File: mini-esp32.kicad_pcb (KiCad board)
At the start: 4 copper layers, 29 x 58 mm, 52 parts, among them J1 BAT, J2 USB_B_Micro, J5 Conn_01x18, J6 Conn_01x18, Q1 AO3401A, Q2 S8050, Q3 S8050, Q5 AO3400A, Q6 AO3400A, SW1 RESET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

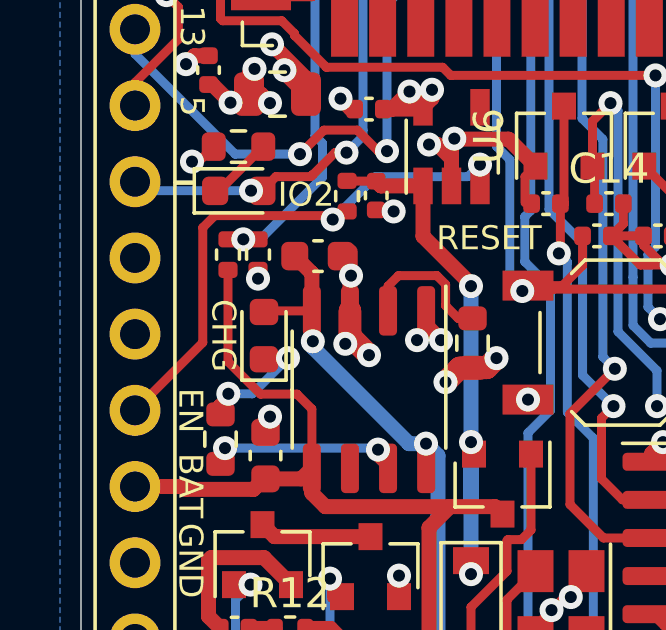
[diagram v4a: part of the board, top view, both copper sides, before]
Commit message: Lower leakage current on battery voltage divider. Add caps.
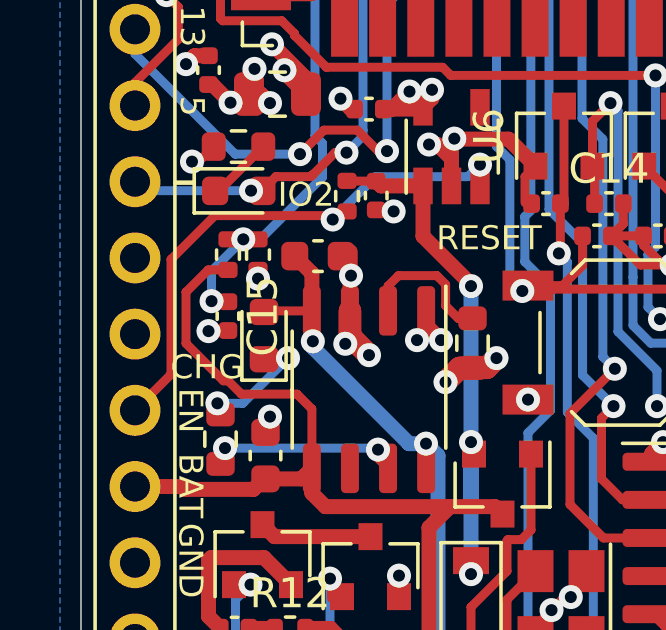
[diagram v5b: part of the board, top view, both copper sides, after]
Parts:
- added C15: 100n, Capacitor_SMD:C_0402_1005Metric, F.Cu at (124.1, 96.4)
- R5, R6: value 100k -> 1M
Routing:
- net I35: track 45.6 -> 48.6 mm, vias 4 -> 5
- net BAT+: track 39.9 -> 41.9 mm
- net GND: track 52.9 -> 53.6 mm, vias 34 -> 35
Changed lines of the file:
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@@
     (thickness 1.6)
     (drawings 81)
-    (tracks 818)
+    (tracks 830)
     (zones 0)
-    (modules 52)
+    (modules 53)
     (nets 79)
   )
@@
   )
   (setup
-    (last_trace_width 0.75)
+    (last_trace_width 0.3)
     (user_trace_width 0.3)
     (user_trace_width 0.5)
@@
       (effects (font (size 1 1) (thickness 0.15)))
     )
-    (fp_text value 100k (at 0 1.17 90) (layer F.Fab)
+    (fp_text value 1M (at 0 1.17 90) (layer F.Fab)
       (effects (font (size 1 1) (thickness 0.15)))
     )
@@
       (effects (font (size 1 1) (thickness 0.15)))
     )
-    (fp_text value 100k (at 0 1.17 90) (layer F.Fab)
+    (fp_text value 1M (at 0 1.17 90) (layer F.Fab)
       (effects (font (size 1 1) (thickness 0.15)))
     )
@@
     )
   )
+  (module Capacitor_SMD:C_0402_1005Metric (layer F.Cu)
+    (at 124.1 96.4 270)
+    (descr "Capacitor SMD 0402 (1005 Metric), square (rectangular) end terminal, IPC_7351 nominal, (Body size source: IPC-SM-782 page 76, https://www.pcb-3d.com/wordpress/wp-content/uploads/ipc-sm-782a_amendment_1_and_2.pdf), generated with kicad-footprint-generator")
+    (tags capacitor)
+    (attr smd)
+    (fp_text reference C15 (at 0 -1.16 90) (layer F.SilkS)
+      (effects (font (size 1 1) (thickness 0.15)))
+    )
+    (fp_text value 100n (at 0 1.16 90) (layer F.Fab)
+      (effects (font (size 1 1) (thickness 0.15)))
+    )
+    (fp_line (start 0.91 0.46) (end -0.91 0.46) (layer F.CrtYd) (width 0.05))
+    (fp_line (start 0.91 -0.46) (end 0.91 0.46) (layer F.CrtYd) (width 0.05))
+    (fp_line (start -0.91 -0.46) (end 0.91 -0.46) (layer F.CrtYd) (width 0.05))
+    (fp_line (start -0.91 0.46) (end -0.91 -0.46) (layer F.CrtYd) (width 0.05))
+    (fp_line (start -0.107836 0.36) (end 0.107836 0.36) (layer F.SilkS) (width 0.12))
+    (fp_line (start -0.107836 -0.36) (end 0.107836 -0.36) (layer F.SilkS) (width 0.12))
+    (fp_line (start 0.5 0.25) (end -0.5 0.25) (layer F.Fab) (width 0.1))
+    (fp_line (start 0.5 -0.25) (end 0.5 0.25) (layer F.Fab) (width 0.1))
+    (fp_line (start -0.5 -0.25) (end 0.5 -0.25) (layer F.Fab) (width 0.1))
+    (fp_line (start -0.5 0.25) (end -0.5 -0.25) (layer F.Fab) (width 0.1))
+    (fp_text user %R (at 0 0 90) (layer F.Fab)
+      (effects (font (size 0.25 0.25) (thickness 0.04)))
+    )
+    (pad 1 smd roundrect (at -0.48 0 270) (size 0.56 0.62) (layers F.Cu F.Paste F.Mask) (roundrect_rratio 0.25)
+      (net 41 I35))
+    (pad 2 smd roundrect (at 0.48 0 270) (size 0.56 0.62) (layers F.Cu F.Paste F.Mask) (roundrect_rratio 0.25)
+      (net 2 GND))
+    (model ${KISYS3DMOD}/Capacitor_SMD.3dshapes/C_0402_1005Metric.wrl
+      (at (xyz 0 0 0))
+      (scale (xyz 1 1 1))
+      (rotate (xyz 0 0 0))
+    )
+  )
   (gr_text RST (at 143.8148 112.2426 180) (layer B.SilkS)
     (effects (font (size 0.8 0.8) (thickness 0.15)) (justify mirror))
@@
     (effects (font (size 0.8 0.8) (thickness 0.15)))
   )
-  (gr_text CHG (at 123.95 97.05 270) (layer F.SilkS)
+  (gr_text CHG (at 123.4 98.1) (layer F.SilkS)
     (effects (font (size 0.8 0.8) (thickness 0.15)))
   )
@@
   (segment (start 128.165 97.065) (end 128.800008 97.700008) (width 0.75) (layer F.Cu) (net 2))
   (segment (start 128.165 96.225) (end 128.165 97.065) (width 0.75) (layer F.Cu) (net 2))
+  (via (at 123.450022 96.9) (size 0.8) (drill 0.4) (layers F.Cu B.Cu) (net 2))
+  (segment (start 123.470022 96.88) (end 123.450022 96.9) (width 0.3) (layer F.Cu) (net 2))
+  (segment (start 124.1 96.88) (end 123.470022 96.88) (width 0.3) (layer F.Cu) (net 2))
   (via (at 132.2 105) (size 0.8) (drill 0.4) (layers F.Cu B.Cu) (net 3))
   (segment (start 132.2 104.55) (end 132.2 105) (width 0.5) (layer F.Cu) (net 3))
@@
   (segment (start 133.430003 103.849999) (end 133.880003 103.849999) (width 0.3) (layer F.Cu) (net 8))
   (segment (start 133.399999 103.880003) (end 133.430003 103.849999) (width 0.3) (layer F.Cu) (net 8))
-  (via (at 124.111244 98.988756) (size 0.8) (drill 0.4) (layers F.Cu B.Cu) (net 9))
-  (segment (start 123.75 99.35) (end 124.111244 98.988756) (width 0.3) (layer F.Cu) (net 9))
   (via (at 126.1 97.8) (size 0.8) (drill 0.4) (layers F.Cu B.Cu) (net 9))
-  (segment (start 124.911244 98.988756) (end 126.1 97.8) (width 0.3) (layer B.Cu) (net 9))
-  (segment (start 124.111244 98.988756) (end 124.911244 98.988756) (width 0.3) (layer B.Cu) (net 9))
   (segment (start 125.3375 97.8) (end 125.3 97.8375) (width 0.3) (layer F.Cu) (net 9))
   (segment (start 126.1 97.8) (end 125.3375 97.8) (width 0.3) (layer F.Cu) (net 9))
-  (segment (start 123.75 99.675) (end 123.75 99.35) (width 0.3) (layer F.Cu) (net 9))
+  (segment (start 124.593178 99.306822) (end 123.746147 99.306822) (width 0.3) (layer B.Cu) (net 9))
+  (segment (start 123.75 99.310675) (end 123.746147 99.306822) (width 0.3) (layer F.Cu) (net 9))
+  (segment (start 126.1 97.8) (end 124.593178 99.306822) (width 0.3) (layer B.Cu) (net 9))
+  (segment (start 123.75 99.675) (end 123.75 99.310675) (width 0.3) (layer F.Cu) (net 9))
+  (via (at 123.746147 99.306822) (size 0.8) (drill 0.4) (layers F.Cu B.Cu) (net 9))
   (segment (start 123.825 92.2) (end 125.275 90.75) (width 0.3) (layer F.Cu) (net 10))
   (segment (start 123.6725 92.2) (end 123.825 92.2) (width 0.3) (layer F.Cu) (net 10))
@@
   (segment (start 137.906156 112.822164) (end 137.906156 113.120155) (width 0.261112) (layer F.Cu) (net 13))
   (segment (start 140.832156 109.896164) (end 137.906156 112.822164) (width 0.261112) (layer F.Cu) (net 13))
-  (segment (start 127.46001 93.05001) (end 127.59 93.18) (width 0.3) (layer F.Cu) (net 15))
-  (segment (start 123.65999 93.05001) (end 127.46001 93.05001) (width 0.3) (layer F.Cu) (net 15))
-  (segment (start 121 99.54) (end 123.26 97.28) (width 0.3) (layer F.Cu) (net 15))
-  (segment (start 123.26 93.45) (end 123.65999 93.05001) (width 0.3) (layer F.Cu) (net 15))
-  (segment (start 123.26 97.28) (end 123.26 93.45) (width 0.3) (layer F.Cu) (net 15))
   (segment (start 127.66 93.25) (end 127.59 93.18) (width 0.3) (layer B.Cu) (net 15))
   (via (at 127.59 93.18) (size 0.8) (drill 0.4) (layers F.Cu B.Cu) (net 15))
@@
   (segment (start 129.01999 91.75001) (end 132.100067 91.75001) (width 0.3) (layer B.Cu) (net 15))
   (segment (start 127.59 93.18) (end 129.01999 91.75001) (width 0.3) (layer B.Cu) (net 15))
+  (segment (start 121 99.54) (end 122.200001 98.339999) (width 0.3) (layer F.Cu) (net 15))
+  (segment (start 122.200001 94.509999) (end 123.65999 93.05001) (width 0.3) (layer F.Cu) (net 15))
+  (segment (start 123.65999 93.05001) (end 127.46001 93.05001) (width 0.3) (layer F.Cu) (net 15))
+  (segment (start 127.46001 93.05001) (end 127.59 93.18) (width 0.3) (layer F.Cu) (net 15))
+  (segment (start 122.200001 98.339999) (end 122.200001 94.509999) (width 0.3) (layer F.Cu) (net 15))
   (via (at 137.6 83) (size 0.8) (drill 0.4) (layers F.Cu B.Cu) (net 16))
   (via (at 137.6 75.6) (size 0.8) (drill 0.4) (layers F.Cu B.Cu) (net 16))
@@
   (segment (start 139.4 77.75) (end 139.4 76.889998) (width 0.3) (layer B.Cu) (net 41))
   (segment (start 139.4 76.889998) (end 140.889998 75.4) (width 0.3) (layer B.Cu) (net 41))
+  (segment (start 123.570181 95.92) (end 123.551496 95.901315) (width 0.3) (layer F.Cu) (net 41))
+  (segment (start 124.1 95.92) (end 123.570181 95.92) (width 0.3) (layer F.Cu) (net 41))
+  (segment (start 124.610002 93.84) (end 123.551496 94.898506) (width 0.3) (layer B.Cu) (net 41))
+  (segment (start 123.551496 94.898506) (end 123.551496 95.901315) (width 0.3) (layer B.Cu) (net 41))
+  (via (at 123.551496 95.901315) (size 0.8) (drill 0.4) (layers F.Cu B.Cu) (net 41))
   (via (at 128.8 68.5) (size 0.8) (drill 0.4) (layers F.Cu B.Cu) (net 42))
   (segment (start 128.855001 68.444999) (end 128.8 68.5) (width 0.3) (layer F.Cu) (net 42))
@@
   (segment (start 129.6 113.064968) (end 129.6 114.5) (width 0.5) (layer F.Cu) (net 68))
   (segment (start 122.58 102.08) (end 121 102.08) (width 0.5) (layer F.Cu) (net 68))
-  (segment (start 126.895 101.475) (end 126.895 99.495) (width 0.3) (layer F.Cu) (net 68))
-  (segment (start 126.895 99.495) (end 126.4 99) (width 0.3) (layer F.Cu) (net 68))
-  (segment (start 125.18315 99) (end 124.1 97.91685) (width 0.3) (layer F.Cu) (net 68))
-  (segment (start 124.1 97.91685) (end 124.1 94.86) (width 0.3) (layer F.Cu) (net 68))
-  (segment (start 126.4 99) (end 125.18315 99) (width 0.3) (layer F.Cu) (net 68))
   (segment (start 126.545 101.825) (end 126.895 101.475) (width 0.5) (layer F.Cu) (net 68))
   (segment (start 125.3 101.825) (end 126.545 101.825) (width 0.5) (layer F.Cu) (net 68))
@@
   (segment (start 127.518002 106.81) (end 126.68 106.81) (width 0.5) (layer F.Cu) (net 68))
   (segment (start 129.6 108.891998) (end 127.518002 106.81) (width 0.5) (layer F.Cu) (net 68))
+  (segment (start 126.4 99) (end 124.549327 99) (width 0.3) (layer F.Cu) (net 68))
+  (segment (start 122.700012 97.310016) (end 122.700012 95.599988) (width 0.3) (layer F.Cu) (net 68))
+  (segment (start 123.44 94.86) (end 124.1 94.86) (width 0.3) (layer F.Cu) (net 68))
+  (segment (start 126.895 101.475) (end 126.895 99.495) (width 0.3) (layer F.Cu) (net 68))
+  (segment (start 122.700012 95.599988) (end 123.44 94.86) (width 0.3) (layer F.Cu) (net 68))
+  (segment (start 126.895 99.495) (end 126.4 99) (width 0.3) (layer F.Cu) (net 68))
+  (segment (start 124.106148 98.556821) (end 123.946817 98.556821) (width 0.3) (layer F.Cu) (net 68))
+  (segment (start 124.549327 99) (end 124.106148 98.556821) (width 0.3) (layer F.Cu) (net 68))
+  (segment (start 123.946817 98.556821) (end 122.700012 97.310016) (width 0.3) (layer F.Cu) (net 68))
   (segment (start 127.1 114) (end 127.6 114.5) (width 0.5) (layer F.Cu) (net 69))
   (segment (start 127.1 109.534998) (end 127.1 114) (width 0.5) (layer F.Cu) (net 69))

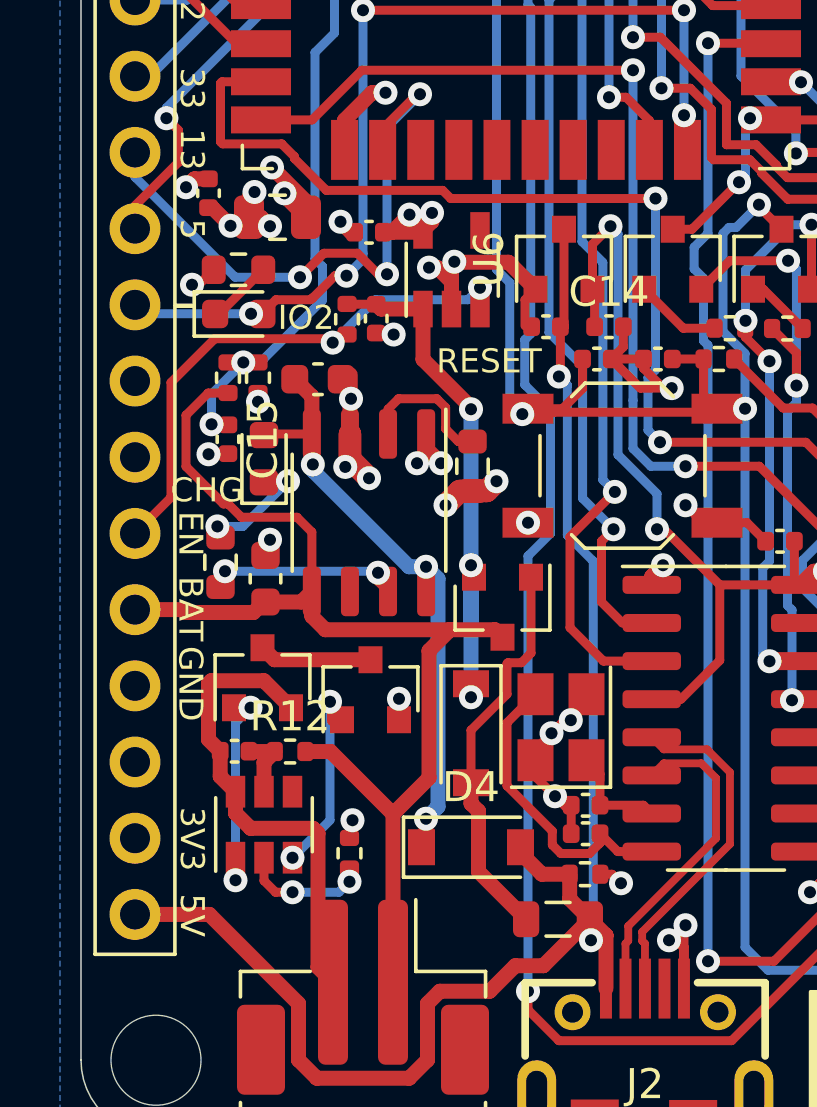
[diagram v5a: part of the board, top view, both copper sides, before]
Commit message: Fix EN pin cap to increase startup delay. Cheaper main bulk cap.
Improve thermals for D4 diode. (For charging)
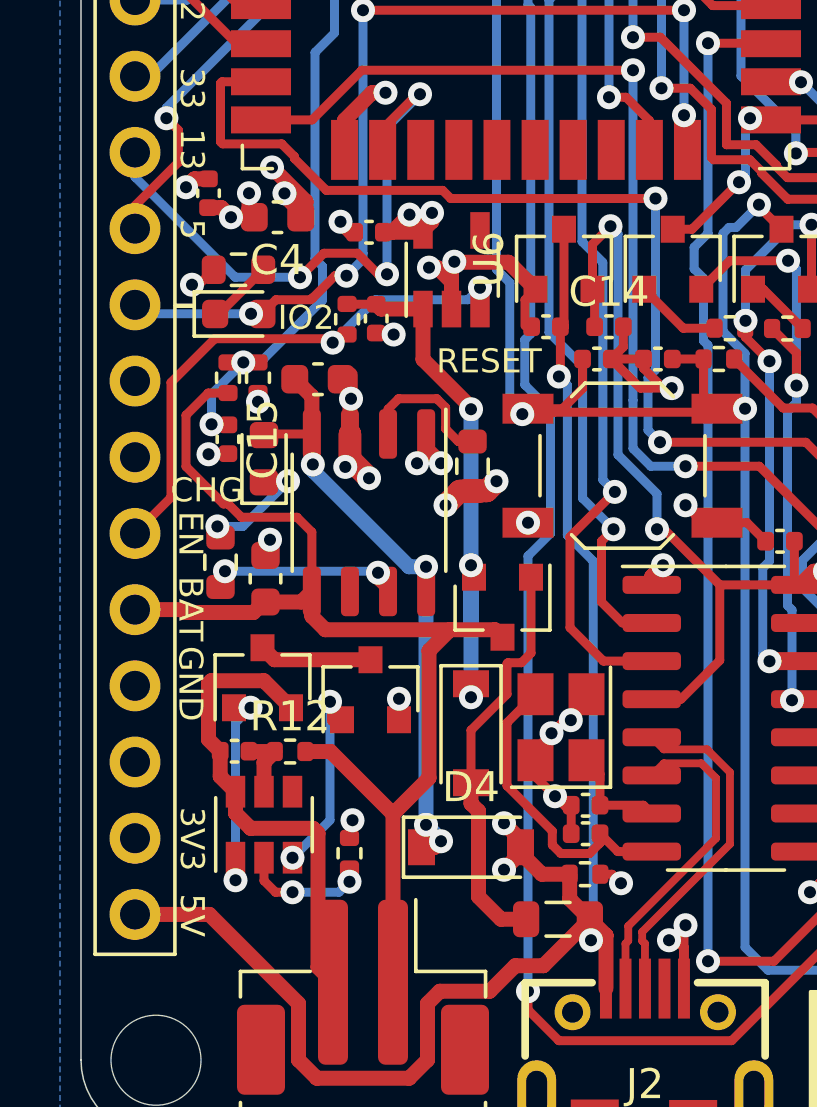
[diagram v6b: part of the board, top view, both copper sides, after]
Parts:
- C4: footprint Capacitor_SMD:C_0805_2012Metric -> Capacitor_SMD:C_0603_1608Metric
- C7: value 100n -> 1u
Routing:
- net VBUS: track 53.3 -> 55.3 mm, vias 2 -> 4
- net GND: track 53.6 -> 52.4 mm, vias 35 -> 34
- net Net-(C1-Pad1): track 19.9 -> 21.0 mm, vias 3 -> 4

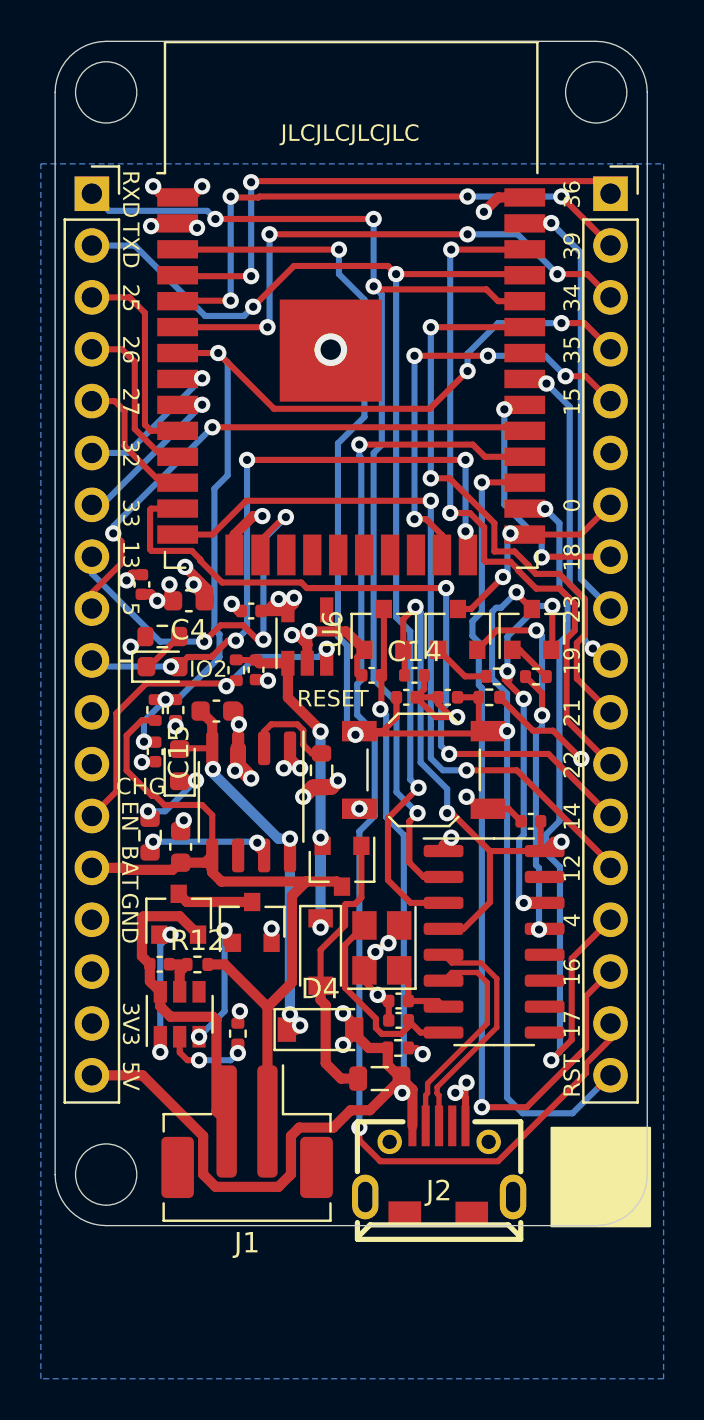
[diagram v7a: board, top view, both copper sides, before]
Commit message: Use TPS3839 instead of battery OC/OD. Lower power usage.
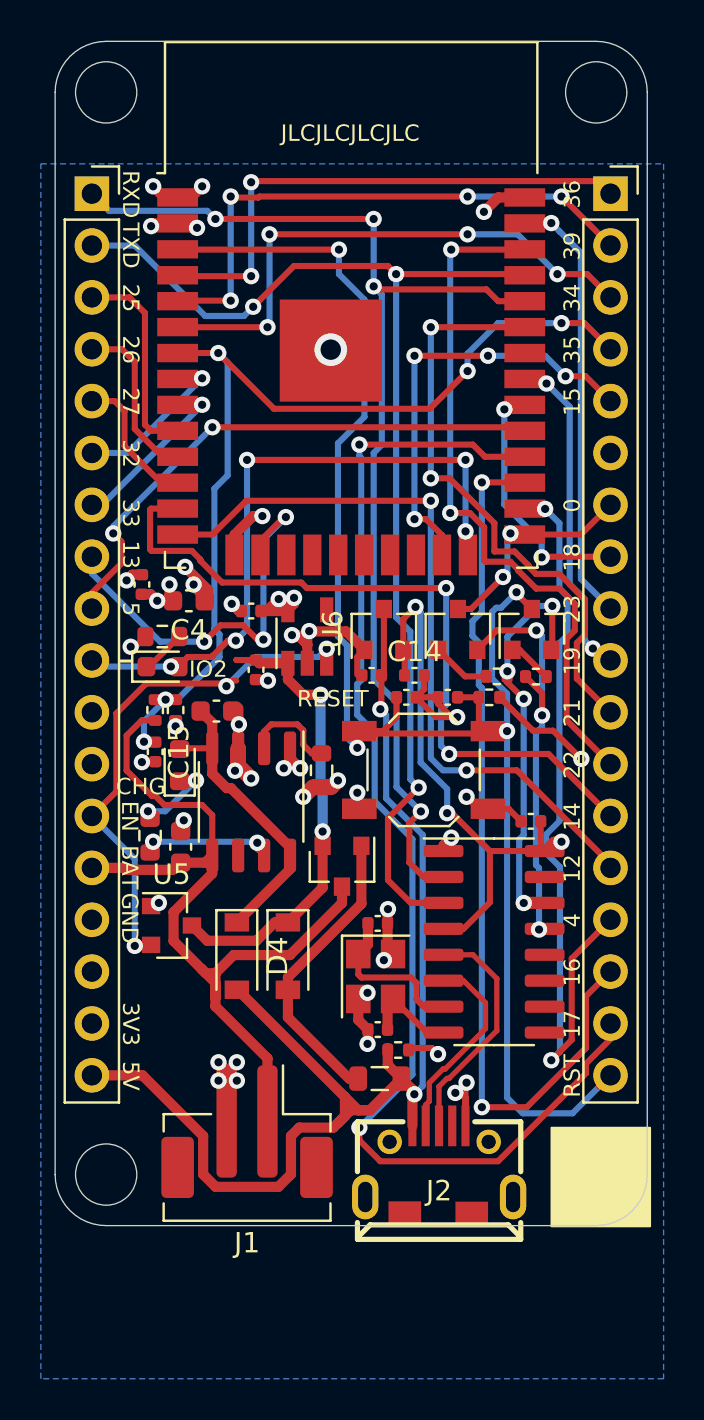
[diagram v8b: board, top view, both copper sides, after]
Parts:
- removed C11: 100n, Capacitor_SMD:C_0402_1005Metric
- removed Q5, Q6: AO3400A, Package_TO_SOT_SMD:SOT-23
- removed R12: 100R, Resistor_SMD:R_0402_1005Metric
- removed R15: 1k, Resistor_SMD:R_0402_1005Metric
- removed R3: 10k, Resistor_SMD:R_0402_1005Metric
- U5: value FS312F-G -> TPS3839K33DBZR; footprint Package_TO_SOT_SMD:SOT-23-6 -> Package_TO_SOT_SMD:SOT-23
- moved D4 5.46 mm to (128.1, 106.4), turned to 270 degrees
- moved U5 4.37 mm to (124.9, 104.9), turned to 0 degrees
- moved C9 3.93 mm to (135.0, 104.8), turned to 0 degrees
- moved D1 1.61 mm to (130.6, 106.4)
- moved Y1 1.43 mm to (134.9, 107.4), turned to 270 degrees
- moved C10 1.11 mm to (135.0, 110.0)
- moved R1 0.10 mm to (136.0, 111.0)
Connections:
- net BAT+ renamed +BATT
- C2 pad 1: Net-(C2-Pad1) -> VCC
- D1 pad 1: Net-(C2-Pad1) -> VCC
- J1 pad 2: BAT- -> GND
- Q1 pad 2: Net-(C2-Pad1) -> VCC
- U2 pad 1: Net-(C2-Pad1) -> VCC
- U5 pad 1: Net-(Q5-Pad1) -> GND
- U5 pad 2: Net-(R15-Pad1) -> EN
- U5 pad 3: Net-(Q6-Pad1) -> VCC
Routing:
- net VCC: track 0.00 -> 22.6 mm, vias 0 -> 2
- net Net-(C2-Pad1): track 19.3 -> 0.00 mm, vias 3 -> 0
- net BAT-: track 16.1 -> 0.00 mm
- net GND: track 52.4 -> 64.2 mm, vias 34 -> 38
- net EN: track 18.6 -> 26.7 mm, vias 2 -> 3
- net Net-(Q5-Pad1): track 7.26 -> 0.00 mm, vias 2 -> 0
- net VBUS: track 55.3 -> 61.7 mm, vias 4 -> 2
- net Net-(Q6-Pad1): track 6.39 -> 0.00 mm, vias 2 -> 0
- net Net-(C1-Pad1): track 21.0 -> 15.1 mm, vias 4 -> 0
- net Net-(C10-Pad1): track 10.2 -> 4.77 mm
- net Net-(C9-Pad1): track 3.53 -> 7.99 mm
- net Net-(R15-Pad1): track 4.36 -> 0.00 mm, vias 2 -> 0
- net Net-(Q5-Pad3): track 3.77 -> 0.00 mm
- net Net-(C11-Pad1): track 2.35 -> 0.00 mm
- net +BATT: track 41.9 -> 44.3 mm
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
